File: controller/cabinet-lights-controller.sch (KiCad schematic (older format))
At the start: 44 parts, among them P1 CONN_01X02, P2 CONN_01X03, T1 Wurth 7447728102, T2 Wurth 750313861, U1 NCP1077, U2 LTV-358T, U3 NCP431

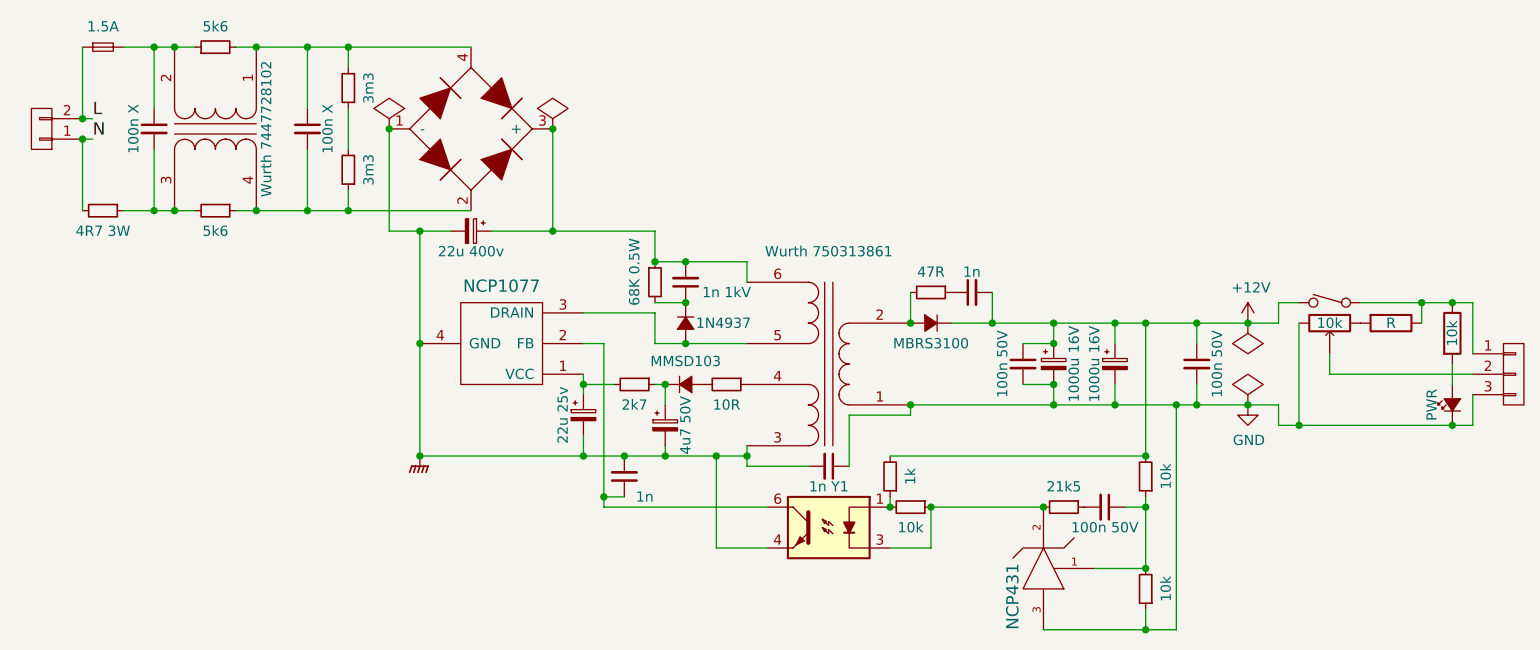
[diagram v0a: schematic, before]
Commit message: More schematic wrangling
Parts for light module
Initial PCB for light module
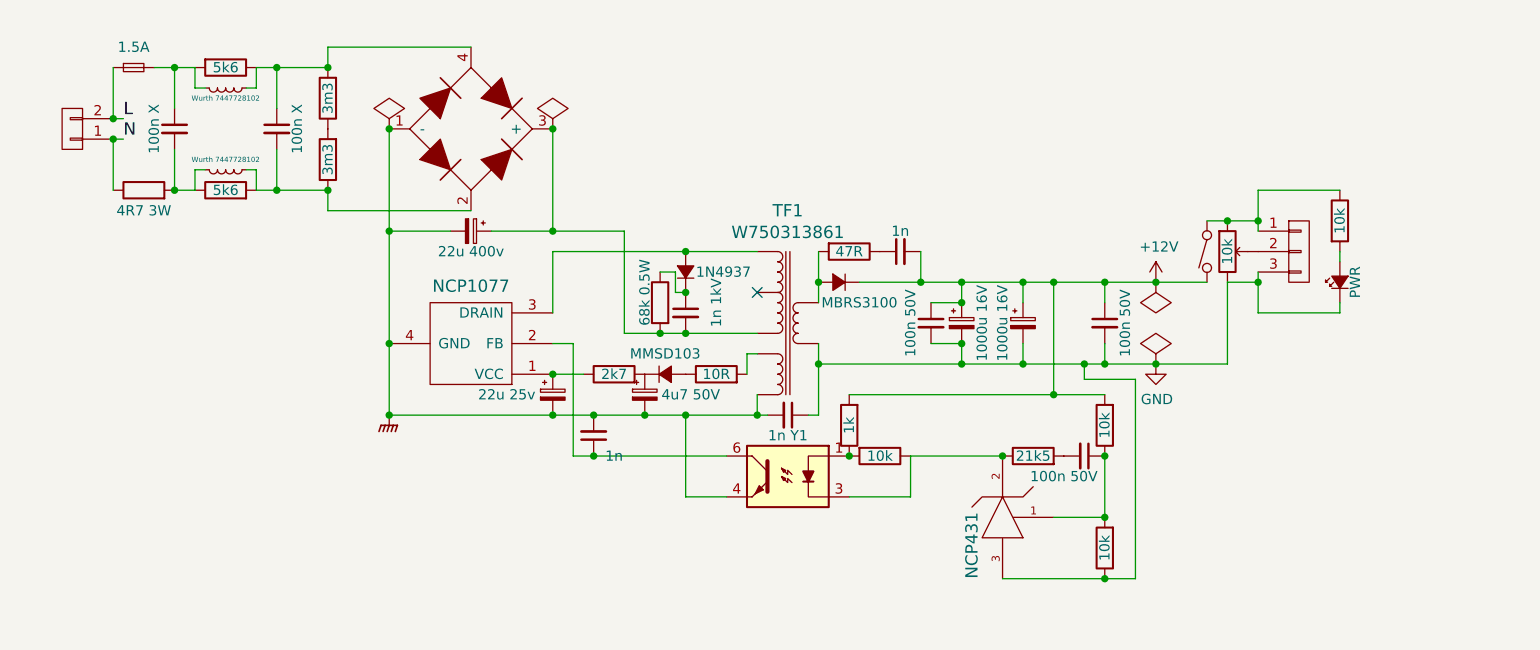
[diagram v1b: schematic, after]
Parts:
- removed R1, R5: 5k6, symbol R_Small
- removed R10: 10R, symbol R_Small
- removed R11: 1k, symbol R_Small
- removed R12, R13, R15: 10k, symbol R_Small
- removed R14: 21k5, symbol R_Small
- removed R2, R3: 3m3, symbol R_Small
- removed R4: 4R7 3W, symbol R_Small
- removed R6: 68K 0.5W, symbol R_Small
- removed R7: 47R, symbol R_Small
- removed R9: 2k7, symbol R_Small
- removed T1: Wurth 7447728102, symbol TRANSFO
- removed T2: Wurth 750313861, symbol TRANSFO2
- added L1, L2: Wurth 7447728102, symbol L_Small
- added R1: 4R7 3W, symbol R
- added R10, R13, R14: 10k, agg:0805, symbol R
- added R11: 47R, agg:0805, symbol R
- added R12: 21k5, agg:0805, symbol R
- added R2, R3: 5k6, agg:0805, symbol R
- added R4, R5: 3m3, agg:0805, symbol R
- added R6: 2k7, agg:0805, symbol R
- added R7: 68k 0.5W, symbol R
- added R9: 1k, agg:0805, symbol R
- added TF1: W750313861, parts:W750313861, symbol W750313861
- D5: renamed from D?; footprint (none) -> LEDs:LED-3MM
- R16: renamed from R?; footprint (none) -> agg:0805
- R8: value R -> 10R; footprint (none) -> agg:0805
- U1: footprint (none) -> TO_SOT_Packages_SMD:SOT-223
- U2: footprint MFSOP-6 -> (none)
- gave numbers to parts that had none: 1
- renumbered C6 to C10, C7 to C11, C8 to C12, C14 to C13, C9 to C14, C10 to C4, C12 to C5, C11 to C6, C4 to C7, C13 to C8, C5 to C9, D4 to D2, D2 to D3, D3 to D4
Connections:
- net +12V: now also R13.2, R9.2
- net GND: now also R14.1, TF1.1
- net GNDPWR: now also TF1.6
- net N: now also R1.1
- net at P2.1 (P1), R16.1, U4.5: now also U4.1; no longer R8.1
- net at R8.2: now also TF1.8; no longer U4.1
- net at C1.1, F1.2: now also L1.2, R2.2
- net at C1.2: now also L2.2, R1.2, R3.1
- net at C2.1, D1.4: now also L1.1, R2.1, R4.2
- net at C2.2, D1.2: now also L2.1, R3.2, R5.1
- net at C3.1, C7.2, D1.3 (+): now also R7.2, TF1.6
- net at C4.1, U1.1 (VCC): now also R6.1
- net at D3.2 (A), U1.3 (DRAIN): now also TF1.10
- net at D4.2 (A): now also R11.2, TF1.5
- net at C6.1, D2.1 (K): now also R6.2
- net at U2.1: now also R10.2, R9.1
- net at U2.3, U3.2: now also R10.1, R12.1
- net at D2.2 (A): now also R8.1
- net at C7.1, D3.1 (K): now also R7.1
- net at C9.1: now also R11.1
- net at C13.1, U3.1: now also R13.1, R14.2
- net at C13.2: now also R12.2
- new net: R4.1, R5.2
- no-connect marks 0 -> 1

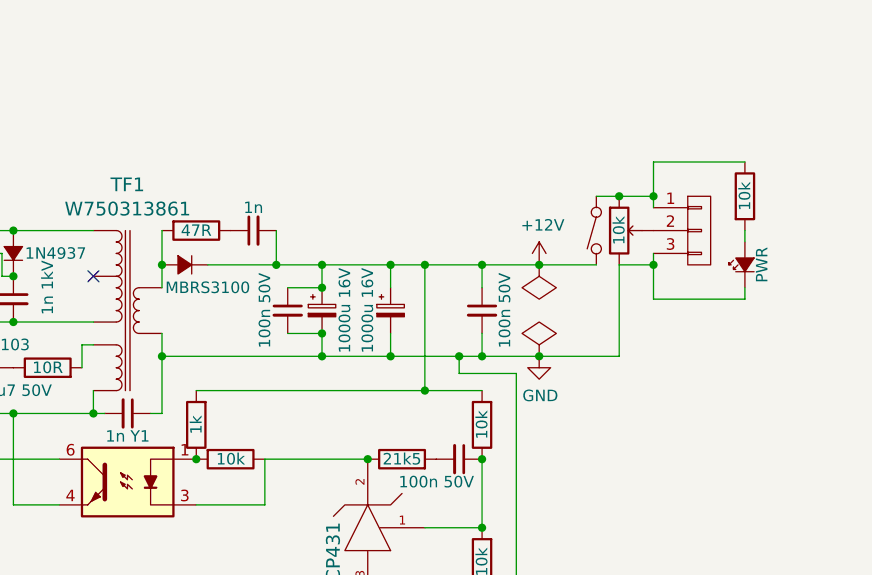
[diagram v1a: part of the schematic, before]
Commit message: Part for pot, transistor driver due to current limits
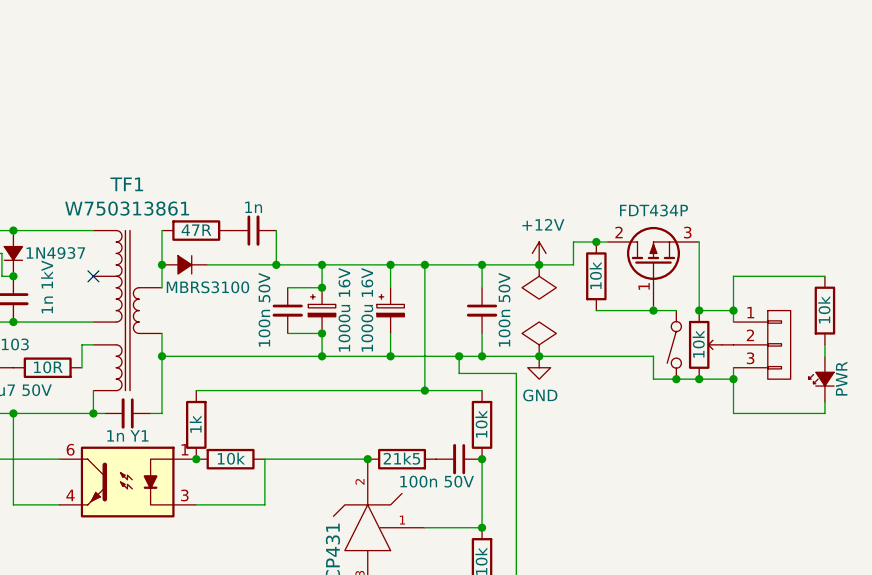
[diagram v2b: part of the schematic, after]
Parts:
- added Q?: FDT434P, TO_SOT_Packages_SMD:SOT-223, symbol Q_PMOS_GDS
- added R?: 10k, symbol R
- U4: Digikey (none) -> 987-1739-ND
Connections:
- net +12V: now also Q?.2 (D), R?.1; no longer U4.4
- net GND: now also U4.4
- net at P2.1 (P1), R16.1, U4.1: now also Q?.3 (S); no longer U4.5
- new net: Q?.1 (G), R?.2, U4.5
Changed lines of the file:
@@
 L CONN_01X03 P2
 U 1 1 577A3B9E
-P 8050 3100
-F 0 "P2" H 8128 3095 50  0001 L CNN
-F 1 "CONN_01X03" H 8128 3050 50  0001 L CNN
-F 2 "" H 8050 3100 50  0001 C CNN
-F 3 "" H 8050 3100 50  0000 C CNN
-	1    8050 3100
+P 8400 3600
+F 0 "P2" H 8478 3595 50  0001 L CNN
+F 1 "CONN_01X03" H 8478 3550 50  0001 L CNN
+F 2 "" H 8400 3600 50  0001 C CNN
+F 3 "" H 8400 3600 50  0000 C CNN
+	1    8400 3600
 	1    0    0    -1
 $EndComp
@@
 L R R16
 U 1 1 577A5366
-P 8250 2950
-F 0 "R16" H 8320 2996 50  0001 L CNN
-F 1 "10k" V 8250 2950 50  0000 C CNN
-F 2 "agg:0805" V 8180 2950 50  0001 C CNN
-F 3 "" H 8250 2950 50  0000 C CNN
-	1    8250 2950
+P 8600 3450
+F 0 "R16" H 8670 3496 50  0001 L CNN
+F 1 "10k" V 8600 3450 50  0000 C CNN
+F 2 "agg:0805" V 8530 3450 50  0001 C CNN
+F 3 "" H 8600 3450 50  0000 C CNN
+	1    8600 3450
 	1    0    0    -1
 $EndComp
@@
 L Led_Small D5
 U 1 1 577A54CE
-P 8250 3250
-F 0 "D5" V 8296 3182 50  0001 R CNN
-F 1 "PWR" H 8250 3175 50  0000 C CNN
-F 2 "LEDs:LED-3MM" V 8250 3250 50  0001 C CNN
-F 3 "" V 8250 3250 50  0000 C CNN
-	1    8250 3250
+P 8600 3750
+F 0 "D5" V 8646 3682 50  0001 R CNN
+F 1 "PWR" H 8600 3675 50  0000 C CNN
+F 2 "LEDs:LED-3MM" V 8600 3750 50  0001 C CNN
+F 3 "" V 8600 3750 50  0000 C CNN
+	1    8600 3750
 	0    -1   -1   0
 $EndComp
@@
 Connection ~ 7350 3250
 Connection ~ 7350 3650
-Wire Wire Line
-	5900 3250 7600 3250
-Wire Wire Line
-	5700 3650 7700 3650
 Connection ~ 5700 3650
 Connection ~ 3600 2500
@@
 Connection ~ 4400 3000
 Wire Wire Line
-	7000 3650 7000 3650
-Wire Wire Line
 	6600 4700 7250 4700
 Connection ~ 6600 4100
@@
 L POT_SW U4
 U 1 1 577A69A0
-P 7700 3100
-F 0 "U4" H 7532 3153 60  0001 R CNN
-F 1 "10k" V 7700 3100 50  0000 C CNN
-F 2 "" H 7650 3100 60  0001 C CNN
-F 3 "" H 7650 3100 60  0001 C CNN
-	1    7700 3100
+P 8050 3600
+F 0 "U4" H 7882 3653 60  0001 R CNN
+F 1 "10k" V 8050 3600 50  0000 C CNN
+F 2 "" H 8000 3600 60  0001 C CNN
+F 3 "http://www.bitechnologies.com/pdfs/p170.pdf" H 8000 3600 60  0001 C CNN
+F 4 "987-1739-ND" H 8050 3600 60  0001 C CNN "Digikey"
+	1    8050 3600
 	1    0    0    -1
 $EndComp
@@
 	5700 3550 5700 3900
 Wire Wire Line
-	6850 3800 6850 3250
+	6850 3250 6850 3800
 Connection ~ 6850 3800
 Connection ~ 6850 3250
@@
 Connection ~ 5050 3300
 Wire Wire Line
-	7600 2950 7850 2950
-Wire Wire Line
-	7700 3650 7700 3250
-Wire Wire Line
-	7850 2800 7850 3000
-Connection ~ 7700 2950
-Wire Wire Line
-	7700 3250 7850 3250
-Wire Wire Line
-	7850 3200 7850 3400
-Wire Wire Line
-	7850 3400 8250 3400
-Connection ~ 7850 3250
-Wire Wire Line
-	8250 3400 8250 3350
-Wire Wire Line
-	8250 3150 8250 3100
-Wire Wire Line
-	8250 2800 7850 2800
-Connection ~ 7850 2950
+	8200 3300 8200 3500
+Wire Wire Line
+	7850 3750 8200 3750
+Wire Wire Line
+	8200 3700 8200 3900
+Wire Wire Line
+	8200 3900 8600 3900
+Connection ~ 8200 3750
+Wire Wire Line
+	8600 3900 8600 3850
+Wire Wire Line
+	8600 3650 8600 3600
+Wire Wire Line
+	8600 3300 8200 3300
+Connection ~ 8200 3450
+Wire Wire Line
+	8050 3450 8200 3450
+$Comp
+L Q_PMOS_GDS Q?
+U 1 1 577D1AA5
+P 7850 3250
+F 0 "Q?" V 8178 3250 50  0001 C CNN
+F 1 "FDT434P" V 8086 3250 50  0000 C CNN
+F 2 "TO_SOT_Packages_SMD:SOT-223" H 8050 3350 50  0001 C CNN
+F 3 "http://www.farnell.com/datasheets/1725655.pdf" H 7850 3250 50  0001 C CNN
+F 4 "1611577" V 7850 3250 60  0001 C CNN "Farnell"
+	1    7850 3250
+	0    -1   -1   0
+$EndComp
+Wire Wire Line
+	8050 3150 8050 3450
+Connection ~ 8050 3450
+$Comp
+L R R?
+U 1 1 577D1BD5
+P 7600 3300
+F 0 "R?" H 7670 3346 50  0001 L CNN
+F 1 "10k" V 7600 3300 50  0000 C CNN
+F 2 "" V 7530 3300 50  0000 C CNN
+F 3 "" H 7600 3300 50  0000 C CNN
+	1    7600 3300
+	1    0    0    -1
+$EndComp
+Wire Wire Line
+	7500 3150 7650 3150
+Wire Wire Line
+	7600 3450 7950 3450
+Connection ~ 7850 3450
+Connection ~ 8050 3750
+Connection ~ 7600 3150
+Wire Wire Line
+	5700 3650 7850 3650
+Wire Wire Line
+	5900 3250 7500 3250
+Wire Wire Line
+	7500 3250 7500 3150
+Wire Wire Line
+	7850 3650 7850 3750
+Connection ~ 7950 3750
 $EndSCHEMATC

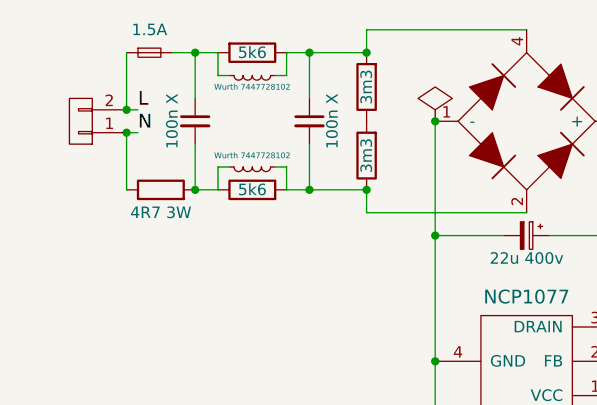
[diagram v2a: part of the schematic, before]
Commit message: Adding more bits for the controller
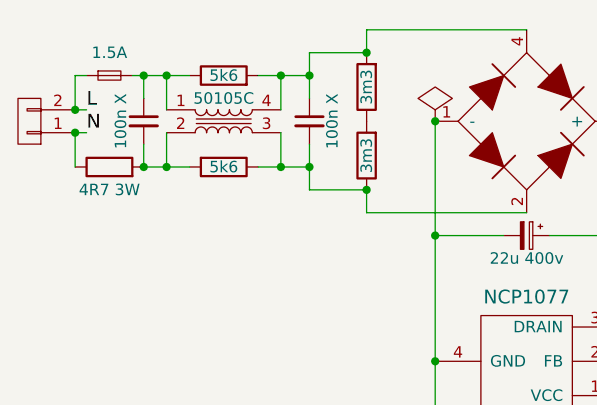
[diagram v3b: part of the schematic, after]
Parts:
- removed L1, L2: Wurth 7447728102, symbol L_Small
- added TR?: 50105C, parts:50xxxC, symbol 50105C
- D1: Farnell (none) -> 1861431
- U4: footprint (none) -> parts:P170xP1
- gave numbers to parts that had none: 2
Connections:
- net at C1.1, F1.2: now also R3.1, TR?.1; no longer R2.2
- net at C1.2, R1.2: now also R2.2, TR?.2; no longer R3.1
- net at C2.1, D1.4, R4.2: now also R3.2, TR?.4; no longer R2.1
- net at C2.2, D1.2, R5.1: now also R2.1, TR?.3; no longer R3.2
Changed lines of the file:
@@
 LIBS:pot_sw
 LIBS:w750313861
+LIBS:50105c
 LIBS:cabinet-lights-controller-cache
 EELAYER 25 0
@@
 L CONN_01X02 P1
 U 1 1 577A3E78
-P 2050 2500
-F 0 "P1" H 1969 2317 50  0001 C CNN
-F 1 "CONN_01X02" H 1969 2316 50  0001 C CNN
-F 2 "" H 2050 2500 50  0001 C CNN
-F 3 "" H 2050 2500 50  0000 C CNN
-	1    2050 2500
-	-1   0    0    1
-$EndComp
-Text Label 2300 2450 0    60   ~ 0
+P 1825 2500
+F 0 "P1" H 1744 2317 50  0001 C CNN
+F 1 "CONN_01X02" H 1744 2316 50  0001 C CNN
+F 2 "" H 1825 2500 50  0001 C CNN
+F 3 "" H 1825 2500 50  0000 C CNN
+	1    1825 2500
+	-1   0    0    1
+$EndComp
+Text Label 2075 2450 0    60   ~ 0
 L
-Text Label 2300 2550 0    60   ~ 0
+Text Label 2075 2550 0    60   ~ 0
 N
 $Comp
 L F_Small F1
 U 1 1 577A40A1
-P 2350 2200
-F 0 "F1" H 2350 2385 50  0001 C CNN
-F 1 "1.5A" H 2350 2300 50  0000 C CNN
-F 2 "" H 2350 2200 50  0001 C CNN
-F 3 "" H 2350 2200 50  0000 C CNN
-	1    2350 2200
+P 2175 2300
+F 0 "F1" H 2175 2485 50  0001 C CNN
+F 1 "1.5A" H 2175 2400 50  0000 C CNN
+F 2 "" H 2175 2300 50  0001 C CNN
+F 3 "" H 2175 2300 50  0000 C CNN
+	1    2175 2300
 	1    0    0    -1
 $EndComp
@@
 L C_Small C1
 U 1 1 577A41F7
-P 2550 2500
-F 0 "C1" H 2642 2546 50  0001 L CNN
-F 1 "100n X" V 2450 2500 50  0000 C CNN
-F 2 "" H 2550 2500 50  0001 C CNN
-F 3 "" H 2550 2500 50  0000 C CNN
-	1    2550 2500
+P 2325 2500
+F 0 "C1" H 2417 2546 50  0001 L CNN
+F 1 "100n X" V 2225 2500 50  0000 C CNN
+F 2 "" H 2325 2500 50  0001 C CNN
+F 3 "" H 2325 2500 50  0000 C CNN
+	1    2325 2500
 	1    0    0    -1
 $EndComp
@@
 F 1 "Diode_Bridge" H 4441 2455 50  0001 L CNN
 F 2 "" H 4000 2500 50  0001 C CNN
-F 3 "" H 4000 2500 50  0000 C CNN
+F 3 "http://www.farnell.com/datasheets/1441701.pdf?_ga=1.238681216.1253160071.1453215511" H 4000 2500 50  0001 C CNN
+F 4 "1861431" H 4000 2500 60  0001 C CNN "Farnell"
 	1    4000 2500
 	1    0    0    -1
@@
 $EndComp
 $Comp
-L GND #PWR2
+L GND #PWR3
 U 1 1 577A5E73
 P 7350 3650
-F 0 "#PWR2" H 7350 3400 50  0001 C CNN
+F 0 "#PWR3" H 7350 3400 50  0001 C CNN
 F 1 "GND" H 7355 3477 50  0000 C CNN
 F 2 "" H 7350 3650 50  0000 C CNN
@@
 $EndComp
 $Comp
-L +12V #PWR3
+L +12V #PWR2
 U 1 1 577A5E84
 P 7350 3250
-F 0 "#PWR3" H 7350 3100 50  0001 C CNN
+F 0 "#PWR2" H 7350 3100 50  0001 C CNN
 F 1 "+12V" H 7365 3423 50  0000 C CNN
 F 2 "" H 7350 3250 50  0000 C CNN
@@
 	0    -1   -1   0
 $EndComp
-Connection ~ 2250 2550
+Connection ~ 2025 2550
 Wire Wire Line
 	5700 3100 5700 3350
@@
 	5850 3800 7100 3800
 Wire Wire Line
-	2250 2450 2300 2450
-Connection ~ 2250 2450
-Wire Wire Line
-	2250 2550 2300 2550
+	2025 2450 2075 2450
+Connection ~ 2025 2450
+Wire Wire Line
+	2025 2550 2075 2550
 $Comp
 L POT_SW U4
@@
 F 0 "U4" H 7882 3653 60  0001 R CNN
 F 1 "10k" V 8050 3600 50  0000 C CNN
-F 2 "" H 8000 3600 60  0001 C CNN
+F 2 "parts:P170xP1" H 8000 3600 60  0001 C CNN
 F 3 "http://www.bitechnologies.com/pdfs/p170.pdf" H 8000 3600 60  0001 C CNN
 F 4 "987-1739-ND" H 8050 3600 60  0001 C CNN "Digikey"
@@
 	1    0    0    -1
 $EndComp
-$Comp
-L L_Small L2
-U 1 1 577AFD9F
-P 2800 2700
-F 0 "L2" V 2622 2700 50  0001 C CNN
-F 1 "Wurth 7447728102" V 2750 2700 25  0000 C CNN
-F 2 "" H 2800 2700 50  0001 C CNN
-F 3 "" H 2800 2700 50  0000 C CNN
-	1    2800 2700
-	0    1    1    0
-$EndComp
-$Comp
-L L_Small L1
-U 1 1 577AFE13
-P 2800 2300
-F 0 "L1" V 2622 2300 50  0001 C CNN
-F 1 "Wurth 7447728102" V 2850 2300 25  0000 C CNN
-F 2 "" H 2800 2300 50  0001 C CNN
-F 3 "" H 2800 2300 50  0000 C CNN
-	1    2800 2300
-	0    1    1    0
-$EndComp
-Wire Wire Line
-	2250 2200 2250 2450
-Wire Wire Line
-	2250 2550 2250 2800
 Wire Wire Line
 	3050 2600 3050 2800
-Connection ~ 3050 2800
-Wire Wire Line
-	2550 2600 2550 2800
-Connection ~ 2550 2800
-Wire Wire Line
-	2550 2200 2550 2400
-Connection ~ 2550 2200
-Wire Wire Line
-	3050 2200 3050 2400
-Connection ~ 3050 2200
 Wire Wire Line
 	3300 2100 4000 2100
@@
 L R R2
 U 1 1 577B0D12
-P 2800 2200
-F 0 "R2" H 2870 2246 50  0001 L CNN
-F 1 "5k6" V 2800 2200 50  0000 C CNN
-F 2 "agg:0805" V 2730 2200 50  0001 C CNN
-F 3 "" H 2800 2200 50  0000 C CNN
-	1    2800 2200
+P 2675 2700
+F 0 "R2" H 2745 2746 50  0001 L CNN
+F 1 "5k6" V 2675 2700 50  0000 C CNN
+F 2 "agg:0805" V 2605 2700 50  0001 C CNN
+F 3 "" H 2675 2700 50  0000 C CNN
+	1    2675 2700
 	0    1    1    0
 $EndComp
-$Comp
-L R R3
-U 1 1 577B0D2E
-P 2800 2800
-F 0 "R3" H 2870 2846 50  0001 L CNN
-F 1 "5k6" V 2800 2800 50  0000 C CNN
-F 2 "agg:0805" V 2730 2800 50  0001 C CNN
-F 3 "" H 2800 2800 50  0000 C CNN
-	1    2800 2800
-	0    -1   -1   0
-$EndComp
-Wire Wire Line
-	2700 2300 2650 2300
-Wire Wire Line
-	2650 2300 2650 2200
-Wire Wire Line
-	2900 2300 2950 2300
-Wire Wire Line
-	2950 2300 2950 2200
-Wire Wire Line
-	2700 2700 2650 2700
-Wire Wire Line
-	2650 2700 2650 2800
-Wire Wire Line
-	2900 2700 2950 2700
-Wire Wire Line
-	2950 2700 2950 2800
 $Comp
 L R R1
 U 1 1 577B0FCC
-P 2400 2800
-F 0 "R1" H 2470 2846 50  0001 L CNN
-F 1 "4R7 3W" V 2300 2800 50  0000 C CNN
-F 2 "" V 2330 2800 50  0001 C CNN
-F 3 "" H 2400 2800 50  0000 C CNN
-	1    2400 2800
+P 2175 2700
+F 0 "R1" H 2245 2746 50  0001 L CNN
+F 1 "4R7 3W" V 2075 2700 50  0000 C CNN
+F 2 "" V 2105 2700 50  0001 C CNN
+F 3 "" H 2175 2700 50  0000 C CNN
+	1    2175 2700
 	0    -1   -1   0
 $EndComp
-Wire Wire Line
-	2950 2200 3300 2200
-Wire Wire Line
-	2950 2800 3300 2800
-Wire Wire Line
-	2650 2800 2550 2800
-Wire Wire Line
-	2650 2200 2450 2200
 $Comp
 L R R8
@@
 	8050 3450 8200 3450
 $Comp
-L Q_PMOS_GDS Q?
+L Q_PMOS_GDS Q1
 U 1 1 577D1AA5
 P 7850 3250
-F 0 "Q?" V 8178 3250 50  0001 C CNN
+F 0 "Q1" V 8178 3250 50  0001 C CNN
 F 1 "FDT434P" V 8086 3250 50  0000 C CNN
 F 2 "TO_SOT_Packages_SMD:SOT-223" H 8050 3350 50  0001 C CNN
@@
 Connection ~ 8050 3450
 $Comp
-L R R?
+L R R15
 U 1 1 577D1BD5
 P 7600 3300
-F 0 "R?" H 7670 3346 50  0001 L CNN
+F 0 "R15" H 7670 3346 50  0001 L CNN
 F 1 "10k" V 7600 3300 50  0000 C CNN
 F 2 "" V 7530 3300 50  0000 C CNN
@@
 	7850 3650 7850 3750
 Connection ~ 7950 3750
+$Comp
+L 50105C TR?
+U 1 1 57844C83
+P 2675 2500
+F 0 "TR?" H 2675 2400 60  0001 C CNN
+F 1 "50105C" H 2675 2600 50  0000 C CNN
+F 2 "parts:50xxxC" H 2675 2400 60  0001 C CNN
+F 3 "http://www.farnell.com/datasheets/1484733.pdf" H 2675 2400 60  0001 C CNN
+F 4 "2062865" H 2675 2500 60  0001 C CNN "Farnell"
+	1    2675 2500
+	1    0    0    -1
+$EndComp
+$Comp
+L R R3
+U 1 1 577B0D2E
+P 2675 2300
+F 0 "R3" H 2745 2346 50  0001 L CNN
+F 1 "5k6" V 2675 2300 50  0000 C CNN
+F 2 "agg:0805" V 2605 2300 50  0001 C CNN
+F 3 "" H 2675 2300 50  0000 C CNN
+	1    2675 2300
+	0    -1   -1   0
+$EndComp
+Wire Wire Line
+	2825 2700 3050 2700
+Connection ~ 2925 2700
+Wire Wire Line
+	2325 2700 2525 2700
+Connection ~ 2425 2700
+Connection ~ 2425 2300
+Wire Wire Line
+	2825 2300 3050 2300
+Connection ~ 2925 2300
+Wire Wire Line
+	2925 2700 2925 2550
+Connection ~ 3050 2700
+Connection ~ 3050 2300
+Wire Wire Line
+	2925 2450 2925 2300
+Wire Wire Line
+	3050 2800 3300 2800
+Wire Wire Line
+	3050 2200 3050 2400
+Wire Wire Line
+	3050 2200 3300 2200
+Wire Wire Line
+	2425 2700 2425 2550
+Connection ~ 2325 2700
+Connection ~ 2325 2300
+Wire Wire Line
+	2425 2450 2425 2300
+Wire Wire Line
+	2275 2300 2525 2300
+Wire Wire Line
+	2325 2300 2325 2400
+Wire Wire Line
+	2325 2600 2325 2700
+Wire Wire Line
+	2075 2300 2025 2300
+Wire Wire Line
+	2025 2300 2025 2450
+Wire Wire Line
+	2025 2550 2025 2700
 $EndSCHEMATC
